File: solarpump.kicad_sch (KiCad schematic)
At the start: 71 parts, among them J1 XLR3 Female Line, J10 MotorSens_M, J11 MotorPowr_M, J12 Wire, J13 Wire, J14 MotorPowr_F, J15 MotorSens_F, J18 2 pin header, J19 2 pin ln/skt, J2 Wire, J20 XLR3 Female Line, J3 Wire, J4 Wire, J5 Soldered, J6 Soldered, J7 Wire, J8 XLR3 Male PCB, J9 XLR3 Male PCB, M1 Motor_DC_ALT, Q1 IRLB8721PBF, Q2 2N3904, Q3 2N3904, Q4 IRLB8721PBF, Q5 IRLB8721PBF, Q6 2N3904, Q7 IRLB8721PBF, Q8 2N3904, SW2 Power On, U1 IR2104, U1_C1 0.1uF, U1_C2 10uF

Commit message: Update for v3
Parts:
- removed +Bat1, -Bat1: Soldered, Connector_Wire:SolderWire-1.5sqmm_1x01_D1.7mm_OD3.9mm, symbol Connector:Conn_01x01_Female
- removed +Bat2, -Bat2: Soldered, Connector_Wire:SolderWire-0.5sqmm_1x01_D0.9mm_OD2.3mm, symbol Connector:Conn_01x01_Female
- removed BT1: 12v AGM 7.2AH, ~, symbol Device:Battery
- removed BT2: LiPo Bat 3V7 300mA, ~, symbol Device:Battery
- removed C11, C5: 220uF 35V, Capacitor_THT:CP_Radial_D8.0mm_P3.50mm, symbol Device:CP
- removed C3, C4, U1_C1: 0.1uF, Capacitor_THT:C_Disc_D5.0mm_W2.5mm_P5.00mm, symbol Device:C
- removed D2: DSS20-0015B, Package_TO_SOT_THT:TO-220-2_Vertical, symbol Device:D_Schottky_ALT
- removed D3: 1N4148, Diode_THT:D_DO-35_SOD27_P7.62mm_Horizontal, symbol Device:D_ALT
- removed D4: 1N4934-E3, Diode_THT:D_DO-41_SOD81_P7.62mm_Horizontal, symbol Device:D_ALT
- removed HS_Q1, HS_Q4, HS_Q5, HS_Q7: H/S, solarpump:Heatsink_14x9.5mm, symbol Mechanical:Heatsink
- removed J1, J20: XLR3 Female Line, ~, symbol Connector:XLR3
- removed J10: MotorSens_M, Connector_PinHeader_1.27mm:PinHeader_1x06_P1.27mm_Vertical, symbol Connector:Conn_01x06_Male
- removed J11: MotorPowr_M, Connector_Phoenix_MC:PhoenixContact_MCV_1,5_2-G-3.5_1x02_P3.50mm_Vertical, symbol Connector:Conn_01x02_Male
- removed J12, J13, J2, J3, J4, J7: Wire, ~, symbol Connector:Conn_01x01_Male
- removed J14: MotorPowr_F, ~, symbol Connector:Conn_01x02_Female
- removed J15: MotorSens_F, ~, symbol Connector:Conn_01x06_Female
- removed J18: 2 pin header, Connector_PinHeader_1.27mm:PinHeader_1x02_P1.27mm_Vertical, symbol Connector:Conn_01x02_Male
- removed J19: 2 pin ln/skt, symbol Connector:Conn_01x02_Female
- removed J5, J6: Soldered, Connector_Wire:SolderWire-0.5sqmm_1x01_D0.9mm_OD2.1mm, symbol Connector:Conn_01x01_Female
- removed J8, J9: XLR3 Male PCB, Connector_Audio:Jack_XLR_Neutrik_NC3FAAH-0_Horizontal, symbol Connector:XLR3
- removed JP3: Disable Q5 (NC), Jumper:SolderJumper-2_P1.3mm_Bridged_Pad1.0x1.5mm, symbol Device:Jumper_NC_Small
- removed L1: 33uH, Inductor_THT:L_Toroid_Vertical_L17.8mm_W8.1mm_P7.62mm_Bourns_5700, symbol Device:L_Core_Iron
- removed M1: Motor_DC_ALT, ~, symbol Motor:Motor_DC_ALT
- removed Q1, Q4, Q5, Q7: IRLB8721PBF, Package_TO_SOT_THT:TO-220-3_Vertical, symbol Transistor_FET:IRLZ34N
- removed Q2, Q3, Q6, Q8: 2N3904, Package_TO_SOT_THT:TO-92_Inline, symbol Transistor_BJT:2N3904
- removed R1, R11, R21, R25, R26, R28, R29, R7: 10K, Resistor_THT:R_Axial_DIN0207_L6.3mm_D2.5mm_P7.62mm_Horizontal, symbol Device:R
- removed R2, R4, R9: 3mOhm, 1W, solarpump:Yageo Shunt Resistor 10x5.2mm, symbol Device:R_Shunt
- removed R8: 220, Resistor_THT:R_Axial_DIN0207_L6.3mm_D2.5mm_P7.62mm_Horizontal, symbol Device:R
- removed S1: FLOW, ~, symbol solarpump:FLOW
- removed SW2: Power On, symbol Switch:SW_Push
- removed TH1, TH2: ED2F103A2-71041, ~, symbol Device:Thermistor
- removed U1: IR2104, Package_DIP:DIP-8_W7.62mm_LongPads, symbol Driver_FET:IR2104
- removed U1_C2: 10uF, Capacitor_THT:C_Disc_D5.0mm_W2.5mm_P5.00mm, symbol Device:C
- added H6, H7, H8: MountingHole, MountingHole:MountingHole_4.3mm_M4, symbol Mechanical:MountingHole
- added J1: 8-way_Screw, TerminalBlock_Phoenix:TerminalBlock_Phoenix_MKDS-3-8-5.08_1x08_P5.08mm_Horizontal, symbol solarpump:Screw_Terminal_01x08_4x2U
- added J2: UART_IO, Connector_PinHeader_2.00mm:PinHeader_1x03_P2.00mm_Vertical, symbol Connector:Conn_01x03_Male
- added J3: AUX_POWER, Connector_PinHeader_2.00mm:PinHeader_1x04_P2.00mm_Vertical, symbol Connector:Conn_01x04_Male
- added J4: USB_A, solarpump:USB_Receptacle_Type_A_GCT, symbol Connector:USB_A
- added J5, J6: Conn_DISP, Connector_PinHeader_2.00mm:PinHeader_2x06_P2.00mm_Vertical, symbol Connector:Conn_01x12_Male
- added NT1: NetTie_2, NetTie:NetTie-2_THT_Pad1.0mm, symbol Device:NetTie_2
- H1, H2, H3, H4, H5: footprint MountingHole:MountingHole_3.5mm -> MountingHole:MountingHole_4.3mm_M4; now in the parts list
- SC1: footprint ~ -> Connector_Wire:SolderWire-1.5sqmm_1x02_P6mm_D1.7mm_OD3mm; DNF (none) -> DNF; now left out of the parts list
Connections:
- net GND: now also J3.1 (Pin_1), J4.4 (GND), J4.5 (Case), J5.12 (Pin_12), J5.6 (Pin_6), NT1.1
- new net +12V: J3.4 (Pin_4)
- new net +3V3: J3.2 (Pin_2), J5.1 (Pin_1), J5.11 (Pin_11)
- new net +5V: J3.3 (Pin_3), J4.1 (VBUS)
- new net FrontPanel/FP_3V3: J6.1 (Pin_1), J6.11 (Pin_11)
- new net FrontPanel/FP_GND: J6.12 (Pin_12), J6.6 (Pin_6)
- new net FrontPanel/I2C_INT: J6.9 (Pin_9)
- new net FrontPanel/I2C_SCL: J6.8 (Pin_8)
- new net FrontPanel/I2C_SDA: J6.7 (Pin_7)
- new net FrontPanel/SPI_CLK: J6.4 (Pin_4)
- new net FrontPanel/SPI_CS: J6.3 (Pin_3)
- new net FrontPanel/SPI_MISO: J6.5 (Pin_5)
- new net FrontPanel/SPI_MOSI: J6.2 (Pin_2)
- new net FrontPanel/~{RESET}: J6.10 (Pin_10)
- new net GNDA: NT1.2
- new net MCU/I2C_INT: J5.9 (Pin_9)
- new net MCU/I2C_SCL: J5.7 (Pin_7)
- new net MCU/I2C_SDA: J5.8 (Pin_8)
- new net MCU/SPI_CLK: J5.4 (Pin_4)
- new net MCU/SPI_CS: J5.3 (Pin_3)
- new net MCU/SPI_MISO: J5.5 (Pin_5)
- new net MCU/SPI_MOSI: J5.2 (Pin_2)
- new net MCU/UART_RX: J2.1 (Pin_1)
- new net MCU/UART_ST: J2.3 (Pin_3)
- new net MCU/UART_TX: J2.2 (Pin_2)
- new net MCU/USB_D+: J4.3 (D+)
- new net MCU/USB_D-: J4.2 (D-)
- new net MCU/~{RESET}: J5.10 (Pin_10)
- new net MPPT/Solr_N: J1.2 (Pin_2)
- new net MPPT/Solr_P: J1.1 (Pin_1)
- new net OUTPUT/Out_Aux+: J1.5 (Pin_5)
- new net OUTPUT/Out_Aux-: J1.6 (Pin_6)
- new net OUTPUT/Out_Pump+: J1.3 (Pin_3)
- new net OUTPUT/Out_Pump-: J1.4 (Pin_4)
- no-connect marks 5 -> 0
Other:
- removed sheet Controller
- added sheet BATTERY (battery.kicad_sch)
- added sheet FrontPanel (frontpanel.kicad_sch)
- added sheet MCU (mcu.kicad_sch)
- added sheet MPPT (mppt.kicad_sch)
- added sheet OUTPUT (output.kicad_sch)
- added sheet PSU (psu.kicad_sch)
- note added: "+VBatt IN; +3V3, +5V, +12V OUT"
- note removed: "(wire)"
- note removed: "12V-36V MPPT, using MCU sensing & PWM control."
- note removed: "2x 4.8mm F spade"
- note removed: "60W 12-18V"
- note removed: "Charger In"
- note removed: "Ext 12V charger"
- note removed: "MOSFET Half bridge driver"
- note removed: "PCB"
- note removed: "Pump Rated 6A 12V"
- note removed: "Solar In"
- note removed: "U1-alternative circuit for MCU drive of Q4, Q5"
- note removed: "Ve(on) = 6V Ve(off) = GND I(on) = 12/20K = 600uA Vbe = ~3V"
- title: Solar Pump Controller -> SolarPump v3

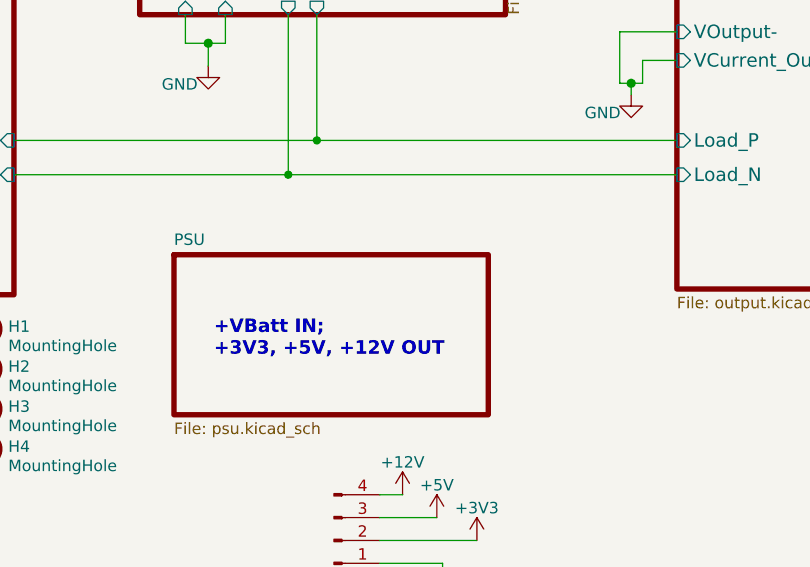
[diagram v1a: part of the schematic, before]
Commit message: Update for Kicad 6-rc; replace 12V reg and cascade; add EEPROM;
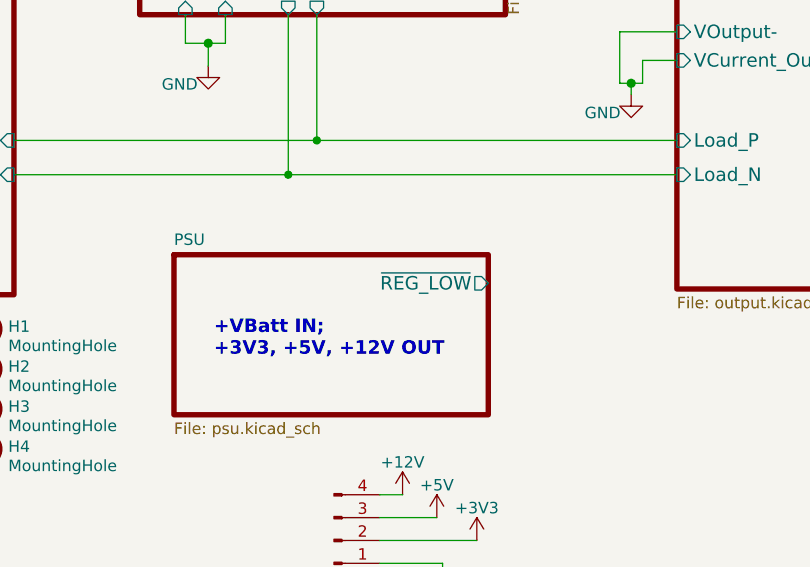
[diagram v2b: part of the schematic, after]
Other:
- sheet PSU ports: added ~{REG_LOW}; removed none

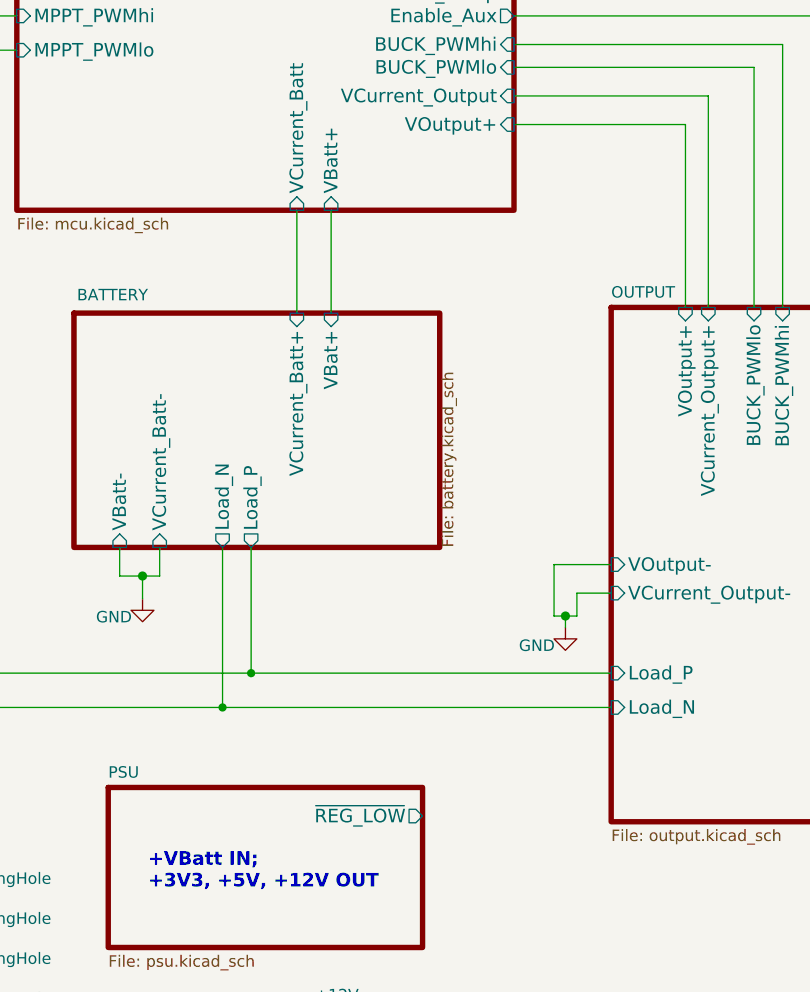
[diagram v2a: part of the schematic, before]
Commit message: Fix diode FP errors, add models; link in regulator error sig; add new coil 3d model; lots of small tweaks
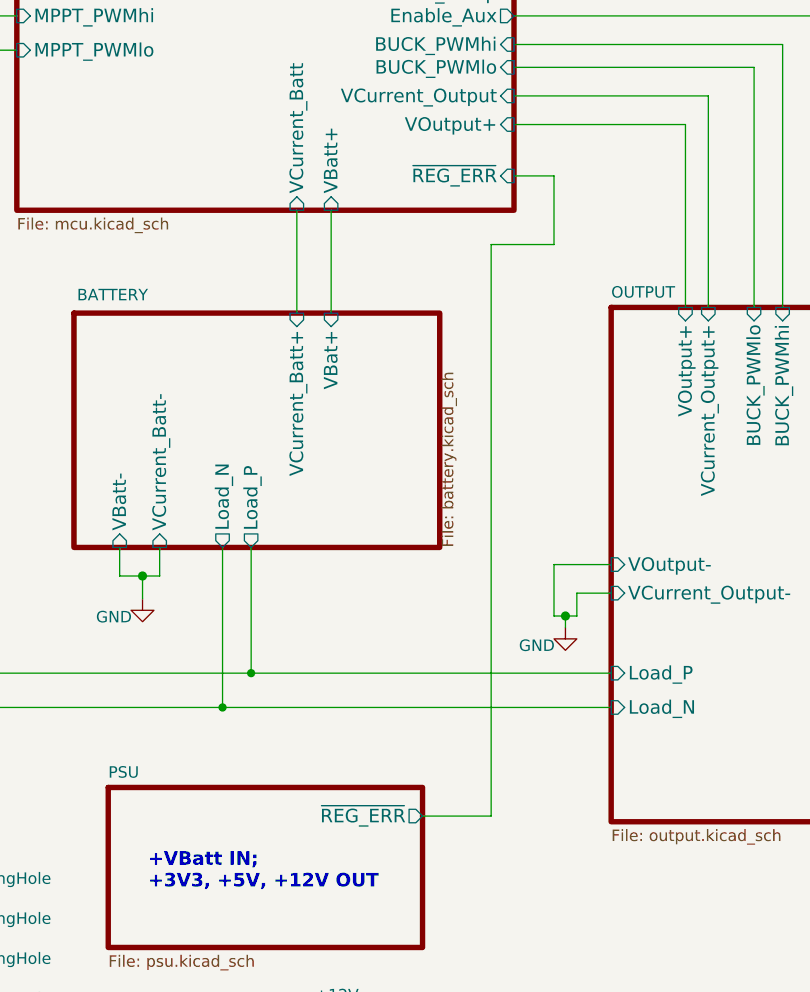
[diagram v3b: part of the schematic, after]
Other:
- sheet MCU ports: added ~{REG_ERR}; removed none
- sheet PSU ports: added ~{REG_ERR}; removed ~{REG_LOW}
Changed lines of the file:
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@@
+    (stroke (width 0) (type default) (color 0 0 0 0))
+  )
+  (wire (pts (xy 170.815 88.9) (xy 166.37 88.9))
     (stroke (width 0) (type default) (color 0 0 0 0))
   )
@@
     (stroke (width 0) (type default) (color 0 0 0 0))
   )
+  (wire (pts (xy 170.815 96.52) (xy 170.815 88.9))
+    (stroke (width 0) (type default) (color 0 0 0 0))
+  )
   (wire (pts (xy 166.37 80.01) (xy 187.96 80.01))
     (stroke (width 0) (type solid) (color 0 0 0 0))
@@
     (stroke (width 0) (type solid) (color 0 0 0 0))
   )
+  (wire (pts (xy 163.83 96.52) (xy 170.815 96.52))
+    (stroke (width 0) (type default) (color 0 0 0 0))
+  )
   (wire (pts (xy 182.88 13.97) (xy 188.595 13.97))
     (stroke (width 0) (type solid) (color 0 0 0 0))
@@
     (stroke (width 0) (type default) (color 0 0 0 0))
   )
+  (wire (pts (xy 156.21 160.02) (xy 163.83 160.02))
+    (stroke (width 0) (type default) (color 0 0 0 0))
+  )
   (wire (pts (xy 219.075 36.195) (xy 231.775 36.195))
     (stroke (width 0) (type solid) (color 0 0 0 0))
@@
   (wire (pts (xy 63.5 50.8) (xy 111.125 50.8))
     (stroke (width 0) (type solid) (color 0 0 0 0))
+  )
+  (wire (pts (xy 163.83 96.52) (xy 163.83 160.02))
+    (stroke (width 0) (type default) (color 0 0 0 0))
   )
   (wire (pts (xy 182.88 15.875) (xy 182.88 13.97))
@@
       (effects (font (size 1.4986 1.4986)) (justify right))
     )
+    (pin "~{REG_ERR}" input (at 166.37 88.9 0)
+      (effects (font (size 1.4986 1.4986)) (justify right))
+    )
   )
   (sheet (at 117.475 104.14) (size 40.64 26.035)
@@
       (effects (font (size 1.27 1.27)) (justify left top))
     )
-    (pin "~{REG_LOW}" output (at 156.21 160.02 0)
+    (pin "~{REG_ERR}" output (at 156.21 160.02 0)
       (effects (font (size 1.4986 1.4986)) (justify right))
     )
@@
     )
     (path "/0cd1335f-feb2-43b1-9360-f076b271f1aa/b11b495a-0db1-499a-ba61-44618793ce10"
-      (reference "D1") (unit 1) (value "S07G-M") (footprint "Diode_SMD:D_SOD-123")
+      (reference "D1") (unit 1) (value "S07G-M") (footprint "Diode_SMD:D_SMF")
     )
     (path "/0cd1335f-feb2-43b1-9360-f076b271f1aa/a3577b91-414e-4bce-a7ad-698eab1a311d"
@@
     )
     (path "/0cd1335f-feb2-43b1-9360-f076b271f1aa/687e6803-1f46-4d00-b2b7-1347b2fe0818"
-      (reference "D3") (unit 1) (value "B140-E3/5AT") (footprint "Diode_SMD:D_SOD-123")
+      (reference "D3") (unit 1) (value "B140-E3/5AT") (footprint "Diode_SMD:D_SMA")
     )
     (path "/0cd1335f-feb2-43b1-9360-f076b271f1aa/bc928855-8470-4e9e-8caf-f78cd0938b8c"
-      (reference "D4") (unit 1) (value "B140-E3/5AT") (footprint "Diode_SMD:D_SOD-123")
+      (reference "D4") (unit 1) (value "B140-E3/5AT") (footprint "Diode_SMD:D_SMA")
     )
     (path "/0cd1335f-feb2-43b1-9360-f076b271f1aa/594a1164-e4f7-4811-8878-5847c399d9a3"
-      (reference "D5") (unit 1) (value "S07G-M") (footprint "Diode_SMD:D_SOD-123")
+      (reference "D5") (unit 1) (value "S07G-M") (footprint "Diode_SMD:D_SMF")
     )
     (path "/e5453b4f-1bdb-42ed-9698-691ee631d9dc/38a39af8-8c40-4c13-ab9c-009f83e935d1"
-      (reference "D6") (unit 1) (value "B140-E3/5AT") (footprint "Diode_SMD:D_SOD-123")
+      (reference "D6") (unit 1) (value "B140-E3/5AT") (footprint "Diode_SMD:D_SMA")
     )
     (path "/e5453b4f-1bdb-42ed-9698-691ee631d9dc/8321a9a7-1adf-427d-9784-9ae465eba1f8"
-      (reference "D7") (unit 1) (value "B140-E3/5AT") (footprint "Diode_SMD:D_SOD-123")
+      (reference "D7") (unit 1) (value "B140-E3/5AT") (footprint "Diode_SMD:D_SMA")
     )
     (path "/e5453b4f-1bdb-42ed-9698-691ee631d9dc/8567c985-0a63-4076-b667-32c819363c72"
-      (reference "D8") (unit 1) (value "B140-E3/5AT") (footprint "Diode_SMD:D_SOD-123")
+      (reference "D8") (unit 1) (value "B140-E3/5AT") (footprint "Diode_SMD:D_SMA")
     )
     (path "/500bedbc-b512-45f8-b103-69cfbdfbee60/f77df2bf-16c5-4593-b8c7-dae6965e0aa4"
-      (reference "D9") (unit 1) (value "B140-E3/5AT") (footprint "Diode_SMD:D_SOD-123")
+      (reference "D9") (unit 1) (value "B140-E3/5AT") (footprint "Diode_SMD:D_SMA")
     )
     (path "/500bedbc-b512-45f8-b103-69cfbdfbee60/7edb0651-6e7c-46de-ad2e-c7b789efa863"
-      (reference "D10") (unit 1) (value "B140-E3/5AT") (footprint "Diode_SMD:D_SOD-123")
+      (reference "D10") (unit 1) (value "B140-E3/5AT") (footprint "Diode_SMD:D_SMA")
     )
     (path "/500bedbc-b512-45f8-b103-69cfbdfbee60/f89fa6e0-88af-41a6-aa57-80042796a362"
-      (reference "D11") (unit 1) (value "S07G-M") (footprint "Diode_SMD:D_SOD-123")
+      (reference "D11") (unit 1) (value "S07G-M") (footprint "Diode_SMD:D_SMF")
     )
     (path "/500bedbc-b512-45f8-b103-69cfbdfbee60/fc4e24c4-2276-46e3-80a8-c94204b238cf"
-      (reference "D12") (unit 1) (value "S07G-M") (footprint "Diode_SMD:D_SOD-123")
+      (reference "D12") (unit 1) (value "S07G-M") (footprint "Diode_SMD:D_SMF")
     )
     (path "/0cd1335f-feb2-43b1-9360-f076b271f1aa/0f0bcc92-a812-43e9-947c-e2f8652c4979"
